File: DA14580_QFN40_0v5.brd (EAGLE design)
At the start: 91 x 72 mm, 26 parts, among them CON1 CON_TC2030-CTL-NL, IC1 IC_SRAM_23K256_256K_32KBSN, IC2 74LVC1G00DBV, IC3 IC_LDO_XX1117, U1 IC_DA14580_QFN40, X1 SSW-114-02-S-S, X2 SSW-114-02-S-S

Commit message: [ FIX ][ 58X ] update schematic with library
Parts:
- IC1: value IC_SRAM_23K256_256K_32KBSN -> IC_MEMORY_8P_AT25XE011_SOP
- IC3: value IC_LDO_XX1117 -> IC_LDO_XX1117_5
- L1: value INDUCTOR_1608 -> 2.2u
- U1: value IC_DA14580_QFN40 -> DA14583-AT2
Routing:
- net GND: track 43.0 -> 41.7 mm
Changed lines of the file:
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@@
 </autorouter>
 <elements>
-<element name="U1" library="mylib" package="QFN40_0.4P5.0X5.0" value="IC_DA14580_QFN40" x="26.2" y="43.1" smashed="yes">
+<element name="U1" library="mylib" package="QFN40_0.4P5.0X5.0" value="DA14583-AT2" x="26.2" y="43.1" smashed="yes">
 <attribute name="NAME" x="22.2" y="46.9" size="1" layer="25" font="vector" ratio="20" align="center"/>
+<attribute name="MOUSER" value="724-DA14583-01AT2" x="26.2" y="43.1" size="1.778" layer="27" display="off"/>
+<attribute name="DIGIKEY" value="" x="26.2" y="43.1" size="1.778" layer="27" display="off"/>
 </element>
 <element name="Q1" library="mylib" package="CR_3216" value="" x="23.5" y="37.2" smashed="yes" rot="R90">
@@
 <attribute name="VALUE" x="27.05" y="39.2" size="1.016" layer="27" rot="R270"/>
 </element>
-<element name="L1" library="mylib" package="L_1608" value="INDUCTOR_1608" x="30.3" y="39.9" smashed="yes" rot="R90">
+<element name="L1" library="mylib" package="L_1608" value="2.2u" x="30.3" y="39.9" smashed="yes" rot="R90">
 <attribute name="NAME" x="32.4" y="40.9" size="1" layer="25" font="vector" ratio="20" rot="R180" align="center"/>
 <attribute name="VALUE" x="32.205" y="39.265" size="1.27" layer="27" rot="R90"/>
@@
 <attribute name="VALUE" x="13.365" y="33.495" size="1.27" layer="27"/>
 </element>
-<element name="IC1" library="mylib" package="IC_08_1.27_150MIL" value="IC_SRAM_23K256_256K_32KBSN" x="27.5" y="28.8" smashed="yes" rot="R270">
+<element name="IC1" library="mylib" package="IC_08_1.27_150MIL" value="IC_MEMORY_8P_AT25XE011_SOP" x="27.5" y="28.8" smashed="yes" rot="R270">
 <attribute name="NAME" x="25" y="32.3" size="1" layer="25" font="vector" ratio="20" align="center"/>
+<attribute name="MOUSER" value="" x="27.5" y="28.8" size="1.778" layer="27" rot="R270" display="off"/>
+<attribute name="DIGIKEY" value="1265-1137-1-ND" x="27.5" y="28.8" size="1.778" layer="27" rot="R270" display="off"/>
 </element>
 <element name="C4" library="mylib" package="C0402" value="" x="28.8" y="32.1" smashed="yes">
@@
 <attribute name="VALUE" x="31.492" y="48.365" size="0.0254" layer="27"/>
 </element>
-<element name="IC3" library="mylib" package="IC_05_0.95_50MIL" value="IC_LDO_XX1117" x="15" y="38.7" smashed="yes" rot="R270">
+<element name="IC3" library="mylib" package="IC_05_0.95_50MIL" value="IC_LDO_XX1117_5" x="15" y="38.7" smashed="yes" rot="R270">
 <attribute name="NAME" x="18.5" y="38" size="1" layer="25" font="vector" ratio="20" align="center"/>
 <attribute name="VALUE" x="11.8" y="38.8" size="1.27" layer="27" font="vector" ratio="16" rot="R270" align="center"/>
@@
 <contactref element="C2" pad="2"/>
 <contactref element="C3" pad="2"/>
-<contactref element="U1" pad="BP"/>
 <contactref element="IC1" pad="4"/>
 <contactref element="IC1" pad="4"/>
@@
 <contactref element="TP6" pad="TP"/>
 <wire x1="28.8" y1="42.1" x2="27.2" y2="42.1" width="0.2" layer="1"/>
-<wire x1="27.2" y1="42.1" x2="26.2" y2="43.1" width="0.2" layer="1"/>
-<wire x1="26.2" y1="43.1" x2="26.2" y2="42" width="0.2" layer="1"/>
 <wire x1="26.2" y1="42" x2="26.4" y2="41.8" width="0.2" layer="1"/>
 <wire x1="26.4" y1="41.8" x2="26.4" y2="40.5" width="0.2" layer="1"/>
@@
 <wire x1="31.4" y1="45.9" x2="31.65" y2="45.65" width="0.6" layer="1"/>
 <wire x1="26.8" y1="45.7" x2="26.8" y2="43.7" width="0.2" layer="1"/>
-<wire x1="26.8" y1="43.7" x2="26.2" y2="43.1" width="0.2" layer="1"/>
 <wire x1="26.4" y1="40.5" x2="26.4" y2="37.5" width="0.2" layer="1"/>
 <contactref element="C9" pad="2"/>
@@
 <wire x1="26.4" y1="52.4" x2="26.4" y2="51.3" width="0.6" layer="1"/>
 <wire x1="26.415" y1="53.95" x2="26.415" y2="53.4" width="0.63" layer="1"/>
-<wire x1="27.3" y1="43.1" x2="26.3" y2="43.1" width="0.8" layer="16"/>
 <contactref element="CON1" pad="5"/>
 <wire x1="32.935" y1="36.27" x2="32.935" y2="36.265" width="0.2" layer="1"/>
@@
 <contactref element="Q2" pad="2"/>
 <contactref element="Q2" pad="4"/>
+<contactref element="U1" pad="BP"/>
+<wire x1="27.3" y1="43.1" x2="26.2" y2="43.1" width="0.8" layer="16"/>
+<wire x1="26.8" y1="43.7" x2="26.2" y2="43.1" width="0.2" layer="1"/>
+<wire x1="26.2" y1="42" x2="26.2" y2="43.1" width="0.2" layer="1"/>
 </signal>
 <signal name="RESET">

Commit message: [ FIX ] library update
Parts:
- added TP2, TP4, TP5: TESTPAD_F, mylib:FIDUCIAL
- IC1: value IC_MEMORY_8P_AT25XE011_SOP -> 1265-1137-1-ND
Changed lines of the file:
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@@
 <attribute name="VALUE" x="13.365" y="33.495" size="1.27" layer="27"/>
 </element>
-<element name="IC1" library="mylib" package="IC_08_1.27_150MIL" value="IC_MEMORY_8P_AT25XE011_SOP" x="27.5" y="28.8" smashed="yes" rot="R270">
-<attribute name="NAME" x="25" y="32.3" size="1" layer="25" font="vector" ratio="20" align="center"/>
+<element name="IC1" library="mylib" package="IC_08_1.27_150MIL" value="1265-1137-1-ND" x="27.5" y="28.8" smashed="yes" rot="R270">
+<attribute name="NAME" x="25" y="32.4" size="1" layer="25" font="vector" ratio="20" align="center"/>
 <attribute name="MOUSER" value="" x="27.5" y="28.8" size="1.778" layer="27" rot="R270" display="off"/>
 <attribute name="DIGIKEY" value="1265-1137-1-ND" x="27.5" y="28.8" size="1.778" layer="27" rot="R270" display="off"/>
@@
 <attribute name="NAME" x="28.8" y="48.2" size="1" layer="25" font="vector" ratio="20"/>
 </element>
+<element name="TP2" library="mylib" package="FIDUCIAL" value="TESTPAD_F" x="-28.6" y="-19.4"/>
+<element name="TP4" library="mylib" package="FIDUCIAL" value="TESTPAD_F" x="-28.6" y="-24"/>
+<element name="TP5" library="mylib" package="FIDUCIAL" value="TESTPAD_F" x="-28.6" y="-28.6"/>
 </elements>
 <signals>

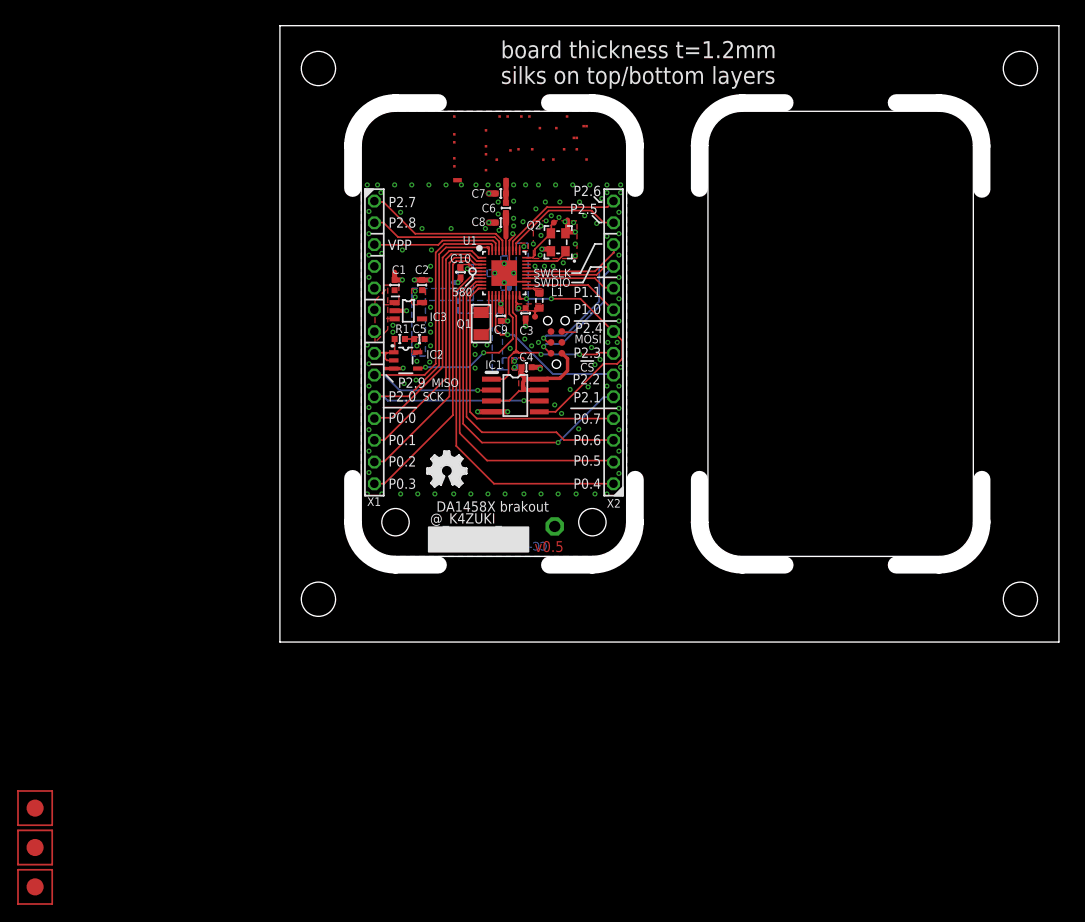
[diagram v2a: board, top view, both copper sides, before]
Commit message: [ 58x ] add fiducial; increase sub board width; move whole board by 1mm North-East; add some value to parts
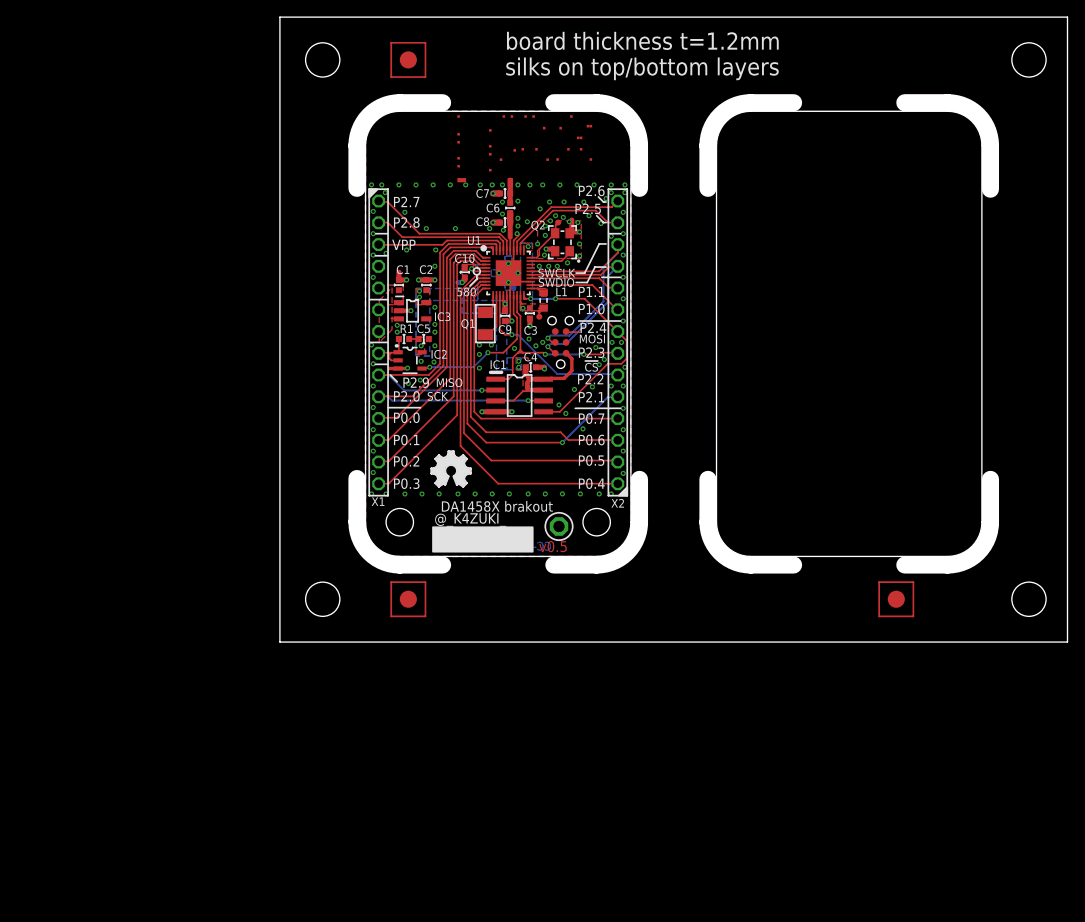
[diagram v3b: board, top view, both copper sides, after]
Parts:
- C1, C2, C3, C9: value (none) -> 1u/1005
- C10, C4, C5: value (none) -> 0.1u/1005
- C6: value (none) -> NM/10p/1005
- C7, C8: value (none) -> NM/1005
- IC2: value 74LVC1G00DBV -> NC7SZ00M5XCT-ND
- Q1: value (none) -> 728-1076-1-ND
- Q2: value (none) -> 887-1833-1-ND
- R1: value (none) -> 10k/1005
- moved TP5 106.1 mm to (72.0, 5.00)
- moved TP2 97.7 mm to (15.0, 68.0)
- moved TP4 52.4 mm to (15.0, 5.00)
- moved C1 0.50 mm to (13.9, 41.7)
- moved C10 0.50 mm to (21.6, 43.2)
- moved C2 0.50 mm to (17.1, 41.7)
- moved C3 0.50 mm to (29.2, 38.4)
- moved C4 0.50 mm to (29.3, 32.1)
- moved C5 0.50 mm to (16.8, 35.4)
- moved C6 0.50 mm to (26.9, 50.7)
- moved C7 0.50 mm to (26.3, 52.4)
- moved C8 0.50 mm to (26.3, 49.0)
- moved C9 0.50 mm to (26.3, 38.1)
- moved CON1 0.50 mm to (32.8, 35.0)
- moved IC1 0.50 mm to (28.0, 28.8)
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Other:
- board size 91 x 72 mm -> 92 x 73 mm

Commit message: [ 58x ] library update
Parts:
- C1, C2, C3, C9: value 1u/1005 -> (none)
- C10, C4, C5: value 0.1u/1005 -> (none)
- C6: value NM/10p/1005 -> NM
- C7, C8: value NM/1005 -> (none)
- L1: value 2.2u -> (none)
- Q1: device mylib:CR_3216 -> mylib:CRYSTAL_FC-135
- R1: value 10k/1005 -> (none)
